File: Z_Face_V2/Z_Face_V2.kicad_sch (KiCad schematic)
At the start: 24 parts, among them J1 CON-5040500591, J4 Conn_01x01, J5 Conn_01x01, J6 Conn_01x01, J7 Conn_01x01, U1 VEML7700, U2 DRV2605LDGS, U3 MCP9808_DFN

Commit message: Added 3-layer coil
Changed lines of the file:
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@@
+	(wire
+		(pts
+			(xy 62.23 148.59) (xy 62.23 151.13)
+		)
+		(stroke
+			(width 0)
+			(type default)
+		)
+	)
 	(wire
 		(pts
@@
 		)
 		(stroke
-			(width 0)
-			(type default)
-		)
-	)
-	(wire
-		(pts
-			(xy 62.23 151.13) (xy 62.23 148.59)
-		)
-		(stroke

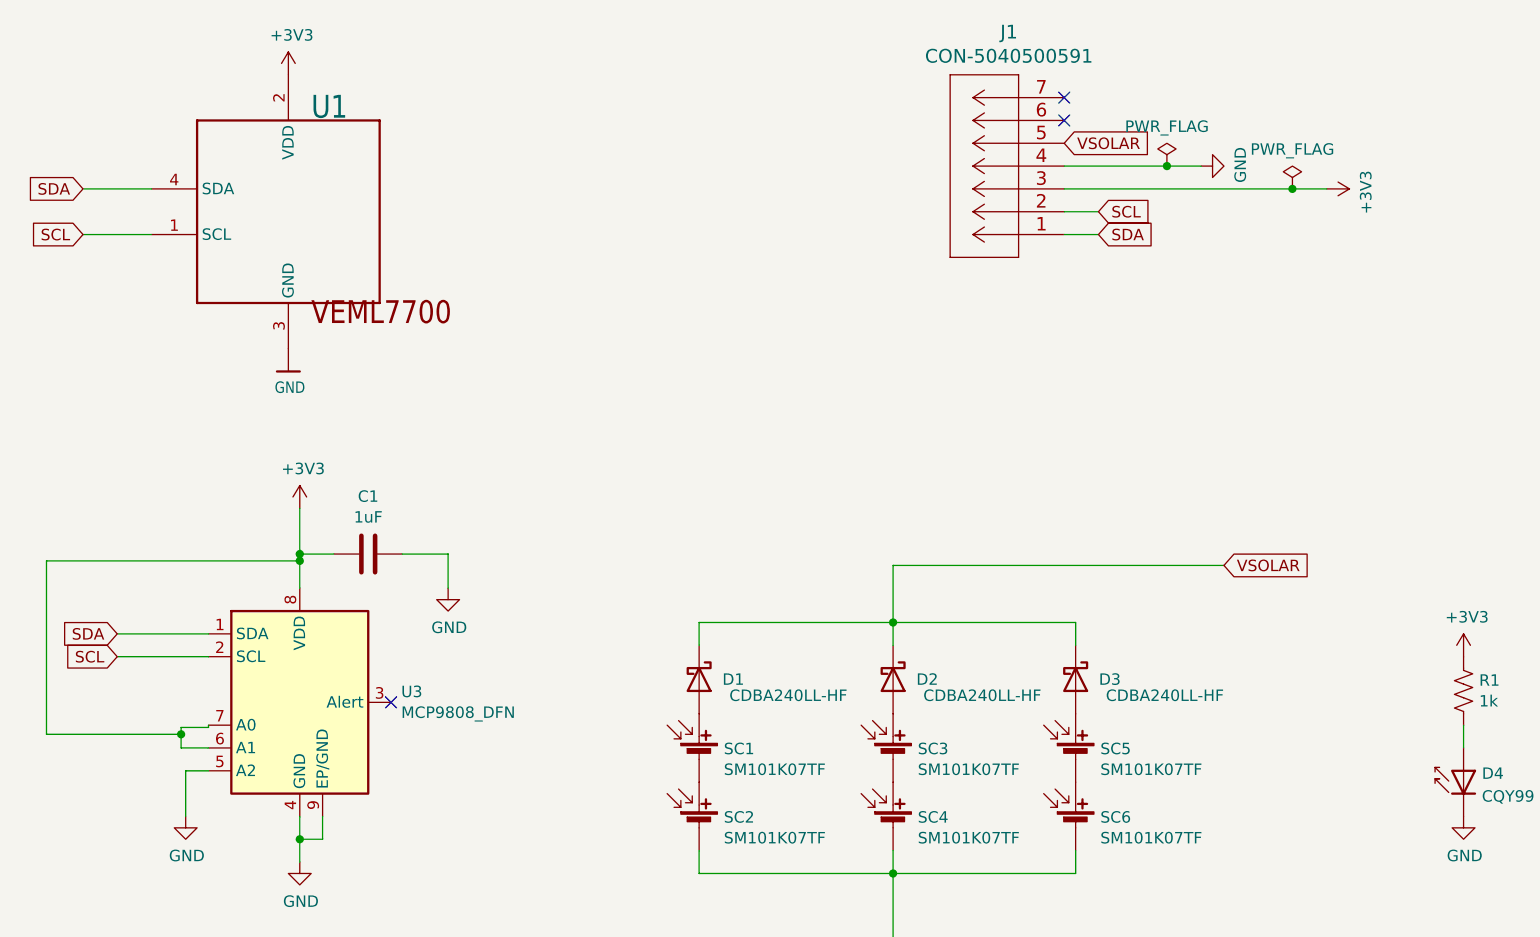
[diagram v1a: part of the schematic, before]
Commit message: Updated Z- Layout Complete
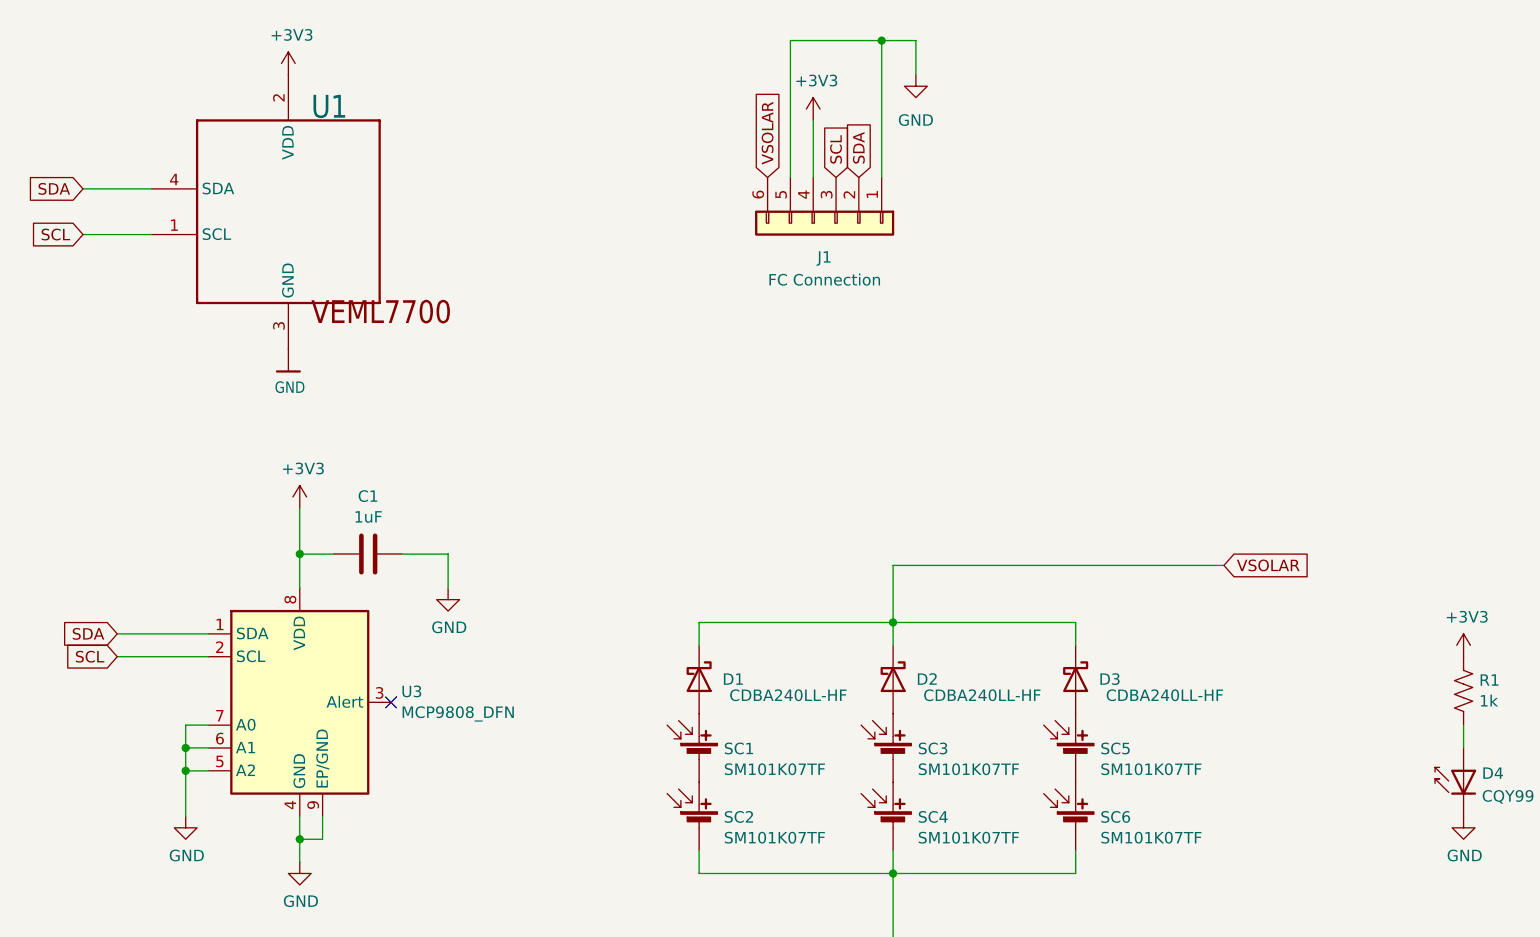
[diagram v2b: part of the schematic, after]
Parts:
- removed J1: CON-5040500591, SolarPanelBoards:CON_5040500591, symbol solar-panel-side-Z-rescue:CON-5040500591-ExtraComponents
- added J1: FC Connection, Molex 6 pos:MOLEX_5040500691, symbol Connector_Generic:Conn_01x06
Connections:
- net +3V3: now also J1.4 (Pin_4); no longer U3.6 (A1), U3.7 (A0)
- net GND: now also U3.6 (A1), U3.7 (A0), J1.1 (Pin_1), J1.5 (Pin_5)
- net SCL: now also J1.3 (Pin_3)
- net SDA: now also J1.2 (Pin_2)
- net VSOLAR: now also J1.6 (Pin_6)
- no-connect marks 8 -> 6

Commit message: Completed V2 Z- Update
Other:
- note added: "NOTE: For BOM Consolidation Initial V2 Production Uses SS34 Schottky Diodes Run a test to ensure the 200mV higher forward voltage doesn't cuase issues with charge circuit."
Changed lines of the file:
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@@
 		(company "CPP BroncoSpace")
+	)
+	(text "NOTE:\nFor BOM Consolidation Initial V2 Production Uses SS34 Schottky Diodes\nRun a test to ensure the 200mV higher forward voltage doesn't\ncuase issues with charge circuit."
+		(exclude_from_sim no)
+		(at 117.348 133.096 0)
+		(effects
+			(font
+				(size 1.27 1.27)
+			)
+		)
 	)
 	(junction

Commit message: Finished Design Tweaks for Z- V2
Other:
- moved on the sheet: C2, C3, D1, D2, D3, D4, J1, R1, SC1, SC2, SC3, SC4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
